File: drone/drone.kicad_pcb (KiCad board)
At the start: 2 copper layers, 62.5 x 72 mm, 32 parts, among them IC1 AT89S4051-P, P1 LeftM, P2 ISP, P3 RightM, P4 Blade1, P5 Blade2, Q1 NPN, Q2 PNP, Q3 NPN, Q4 PNP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

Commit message: Fix the circuit
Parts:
- P3: value RightM -> Blade1
- P4: value Blade1 -> Blade2
- P5: value Blade2 -> RightM
- Q1, Q3, Q5, Q7, Q9: footprint Discret:TO18CBE -> Discret:TO18EBC
- Q2, Q4, Q6, Q8: value PNP -> NPN; footprint Discret:TO18CBE -> Discret:TO18EBC
- R5: value 1K -> 3K3
- R9: value 3K3 -> 1K
- moved Q7 105.3 mm to (252.0, 85.3), turned to 0 degrees
- moved C1 96.7 mm to (249.6, 100.4), turned to 0 degrees
- moved BT1 90.5 mm to (215.0, 74.9), turned to 0 degrees
- moved Q6 85.0 mm to (243.2, 93.8), turned to 0 degrees
- moved R8 83.2 mm to (234.6, 111.6)
- moved P5 74.9 mm to (235.8, 74.9), turned to 0 degrees
- moved Q9 72.4 mm to (243.2, 102.2), turned to 0 degrees
- moved R6 67.0 mm to (217.4, 108.2), turned to 90 degrees
- moved U1 62.7 mm to (196.2, 103.5), turned to 0 degrees
- moved SW2 58.7 mm to (227.0, 90.9), turned to 0 degrees
- moved C2 49.7 mm to (203.9, 79.9)
- moved SW3 46.5 mm to (216.5, 90.9), turned to 0 degrees
- moved R7 43.2 mm to (196.1, 90.5), turned to 0 degrees
- moved R9 39.6 mm to (206.2, 108.7), turned to 0 degrees
- moved IC1 39.5 mm to (164.4, 117.8)
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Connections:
- P3 pad 2: Net-(P3-Pad2) -> GND
- P4 pad 1: Net-(P4-Pad1) -> Net-(P3-Pad1)
- P5 pad 1: Net-(P4-Pad1) -> Net-(P5-Pad1)
- P5 pad 2: GND -> Net-(P5-Pad2)
- Q6 pad 1: GND -> Net-(P5-Pad1)
- Q6 pad 3: Net-(P3-Pad1) -> +12V
- Q7 pad 1: Net-(P3-Pad2) -> GND
- Q7 pad 3: +12V -> Net-(P5-Pad1)
- Q8 pad 1: GND -> Net-(P5-Pad2)
- Q8 pad 3: Net-(P3-Pad2) -> +12V
- Q9 pad 1: Net-(P4-Pad1) -> GND
- Q9 pad 3: +12V -> Net-(P5-Pad2)
- R2 pad 1: LMotor1 -> Net-(Q2-Pad2)
- R2 pad 2: Net-(Q2-Pad2) -> LMotor2
- R4 pad 1: LMotor2 -> LMotor1
- R5 pad 2: RMotor1 -> BladeCon
- R6 pad 1: RMotor1 -> Net-(Q6-Pad2)
- R6 pad 2: Net-(Q6-Pad2) -> RMotor1
- R7 pad 1: RMotor2 -> Net-(Q7-Pad2)
- R7 pad 2: Net-(Q7-Pad2) -> RMotor2
- R9 pad 1: Net-(Q9-Pad2) -> RMotor1
- R9 pad 2: BladeCon -> Net-(Q9-Pad2)
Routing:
- net GND: track 162.6 -> 0.00 mm, vias 1 -> 0
- net +5V: track 102.1 -> 0.00 mm, vias 1 -> 0
- net Net-(P1-Pad1): track 97.0 -> 0.00 mm, vias 3 -> 0
- net +12V: track 96.3 -> 0.00 mm
- net RMotor2: track 66.6 -> 0.00 mm, vias 6 -> 0
- net LMotor2: track 65.6 -> 0.00 mm
- net RMotor1: track 56.4 -> 0.00 mm, vias 2 -> 0
- net LMotor1: track 52.3 -> 0.00 mm, vias 2 -> 0
- net Reset: track 46.2 -> 0.00 mm, vias 1 -> 0
- net Net-(P3-Pad1): track 37.7 -> 0.00 mm, vias 1 -> 0
- net Int0: track 36.2 -> 0.00 mm
- net BladeCon: track 29.4 -> 0.00 mm, vias 2 -> 0
- net Net-(P4-Pad1): track 28.3 -> 0.00 mm
- net Net-(P1-Pad2): track 27.6 -> 0.00 mm
- net Net-(P3-Pad2): track 25.2 -> 0.00 mm
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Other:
- board outline removed
- board text removed: "(c)2015 Henry Schmale"
- board text removed: "+"

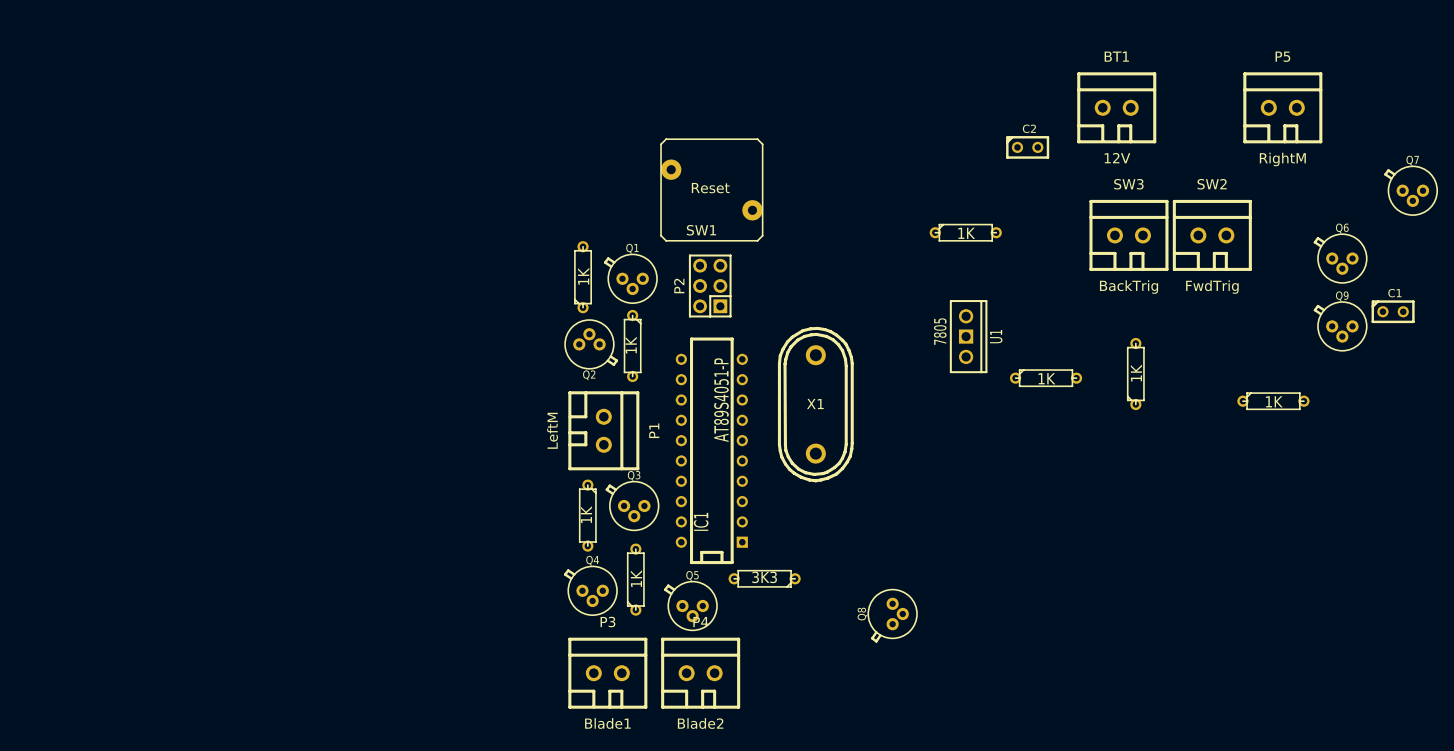
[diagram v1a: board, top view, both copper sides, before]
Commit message: Wrote a real wait function
* Wrote a wait sub that waits for timer0 to overflow R0
* Rerouted the Pcb
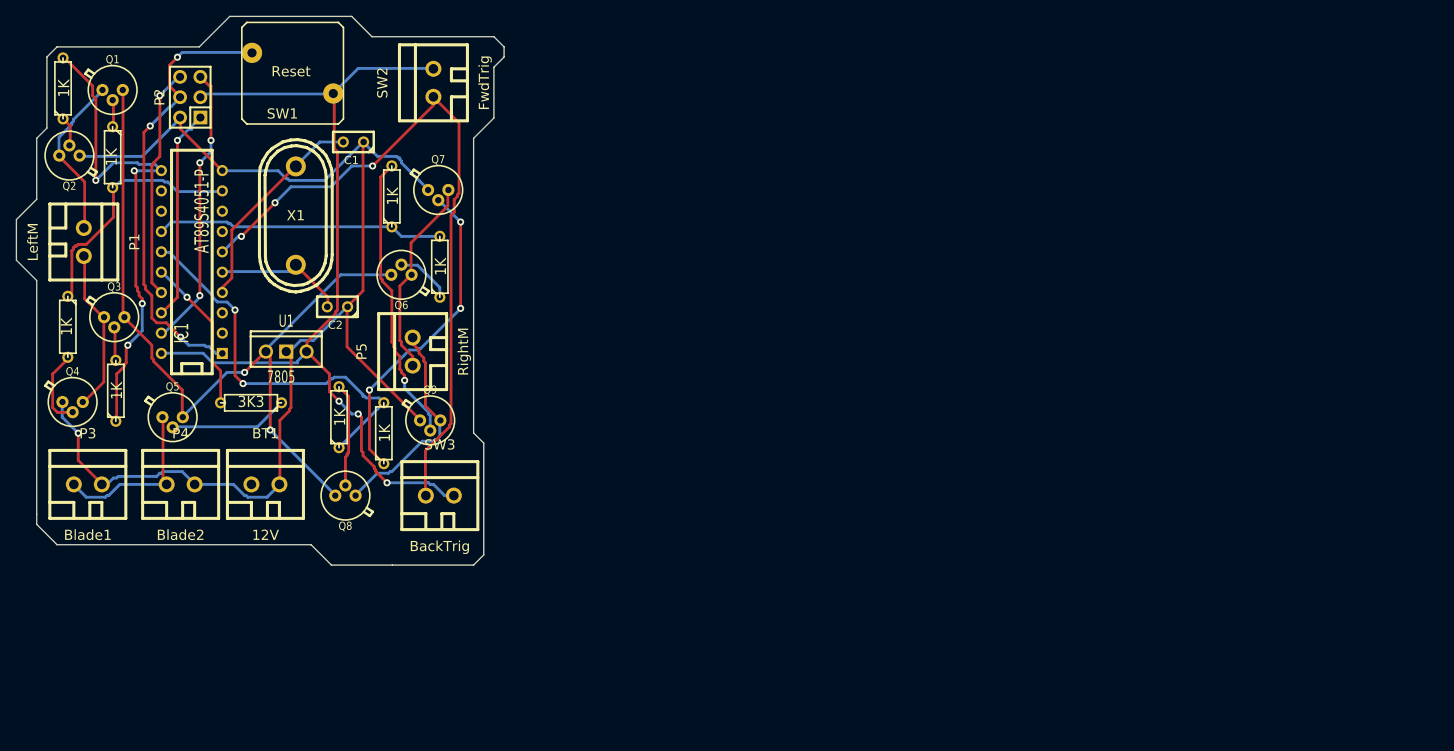
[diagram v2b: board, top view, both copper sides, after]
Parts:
- moved C1 131.7 mm to (119.6, 79.2), turned to 180 degrees
- moved Q7 121.8 mm to (130.2, 85.2)
- moved Q6 117.6 mm to (125.6, 95.8), turned to 180 degrees
- moved R8 116.8 mm to (117.8, 113.6), turned to 90 degrees
- moved BT1 116.4 mm to (108.6, 122.0)
- moved Q9 114.6 mm to (129.2, 114.0)
- moved P5 113.0 mm to (127.0, 105.4), turned to 90 degrees
- moved SW2 99.2 mm to (129.6, 71.8), turned to 90 degrees
- moved SW3 92.1 mm to (130.4, 123.4)
- moved C2 88.5 mm to (117.6, 99.8), turned to 180 degrees
- moved R6 88.0 mm to (130.4, 94.8)
- moved U1 85.0 mm to (111.2, 105.4), turned to 90 degrees
- moved R9 84.9 mm to (124.4, 86.0), turned to 90 degrees
- moved R7 76.9 mm to (123.4, 115.6), turned to 90 degrees
- moved Q8 70.0 mm to (118.6, 123.4), turned to 180 degrees
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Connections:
- BT1 pad 1: +12V -> Net-(BT1-Pad1)
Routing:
- net GND: track 0.00 -> 159.6 mm, vias 0 -> 1
- net +5V: track 0.00 -> 114.8 mm, vias 0 -> 3
- net +12V: track 0.00 -> 99.8 mm, vias 0 -> 2
- net Int0: track 0.00 -> 88.1 mm, vias 0 -> 3
- net LMotor2: track 0.00 -> 63.5 mm, vias 0 -> 4
- net Reset: track 0.00 -> 56.7 mm, vias 0 -> 3
- net RMotor2: track 0.00 -> 49.3 mm, vias 0 -> 2
- net Net-(Q7-Pad2): track 0.00 -> 40.4 mm, vias 0 -> 3
- net Net-(Q9-Pad2): track 0.00 -> 36.2 mm, vias 0 -> 1
- net RMotor1: track 0.00 -> 36.1 mm
- net Net-(IC1-Pad19): track 0.00 -> 35.7 mm, vias 0 -> 3
- net LMotor1: track 0.00 -> 31.5 mm
- net Net-(IC1-Pad17): track 0.00 -> 29.2 mm, vias 0 -> 1
- net Net-(P5-Pad2): track 0.00 -> 27.6 mm
- net Net-(C1-Pad2): track 0.00 -> 26.9 mm
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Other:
- board outline added: 61 x 68.6 mm
